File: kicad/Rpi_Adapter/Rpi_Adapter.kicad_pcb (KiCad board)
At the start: 2 copper layers, 65 x 22 mm, 49 parts, among them P1 CONN_02X20, P2 CONN_02X03

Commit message: Created the layout and submitted to OSH Park
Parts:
- removed 1 (x2), 10, 11, 12, 13, 14, 15, 16, 17, 18, 19, 2, 20 (x2), 21 (x2), 22, 23, 24, 25, 26, 27, 28, 29, 3, 30, 31, 32, 33, 34, 35, 36, 37, 38, 39, 4, 40 (x2), 5, 6, 7, 8, 9: Stitch, Rpi_Adapter_Footprints:Stitch
- removed MCU1: RaspberryPi_3b, Rpi_Adapter_Footprints:Pin_Header_Straight_2x20_Pitch2.54mm
- removed MNT** (x2): MountingHole_2.7mm_M2.5, Mounting_Holes:MountingHole_2.7mm_M2.5
- removed P2: CONN_02X03, Pin_Headers:Pin_Header_Straight_2x03_Pitch2.54mm
- added ?: Stitch, Rpi_Adapter_Footprints:Stitch, F.Cu at (169.6, 42.4)
- added ?: Stitch, Rpi_Adapter_Footprints:Stitch, F.Cu at (167.6, 41.5)
- added ?: Stitch, Rpi_Adapter_Footprints:Stitch, F.Cu at (172.2, 37.6)
- added ?: Stitch, Rpi_Adapter_Footprints:Stitch, F.Cu at (169.5, 40.6)
- added ?: Stitch, Rpi_Adapter_Footprints:Stitch, F.Cu at (171.2, 36.6)
- added ?: Stitch, Rpi_Adapter_Footprints:Stitch, F.Cu at (170.6, 39.1)
- added ?: Stitch, Rpi_Adapter_Footprints:Stitch, F.Cu at (169.5, 38.2)
- added ?: Stitch, Rpi_Adapter_Footprints:Stitch, F.Cu at (168.1, 39.8)
- added ?: Stitch, Rpi_Adapter_Footprints:Stitch, F.Cu at (167.7, 43.3)
- added H1: DIGI_XBEE, Rpi_Adapter_Footprints:XBEE_S2C_Short, F.Cu at (176.0, 45.8)
- P1: value CONN_02X20 -> Raspberry PI; footprint Pin_Headers:Pin_Header_Straight_2x20_Pitch2.54mm -> Socket_Strips:Socket_Strip_Straight_2x06_Pitch2.54mm
- moved P1 7.46 mm to (158.8, 47.2)
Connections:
- P1 pad 1: /5V -> /3V3
- P1 pad 10: GND -> /UART0_Rx
- P1 pad 11: /GPIO_18 -> (no net)
- P1 pad 12: /GPIO_17 -> (no net)
- P1 pad 2: /3V3 -> /5V
- P1 pad 3: /5V -> (no net)
- P1 pad 4: /I2C1_SDA -> /5V
- P1 pad 5: GND -> (no net)
- P1 pad 6: /I2C1_SCL -> GND
- P1 pad 7: /UART0_Tx -> (no net)
- P1 pad 8: /GPIO_4 -> /UART0_Tx
- P1 pad 9: /UART0_Rx -> GND
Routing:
- net /I2C1_SCL: track 31.1 -> 0.00 mm
- net /I2C1_SDA: track 31.1 -> 0.00 mm
- net /GPIO_4: track 25.0 -> 0.00 mm
- net /GPIO_5: track 22.6 -> 0.00 mm
- net /GPIO_6: track 22.6 -> 0.00 mm
- net /5V: track 21.1 -> 2.54 mm
- net /3V3: track 40.1 -> 25.4 mm
- net /GPIO_18: track 9.35 -> 0.00 mm
- net /SPI0_SCLK: track 9.30 -> 0.00 mm
- net /SPI0_MISO: track 9.30 -> 0.00 mm
- net /GPIO_27: track 9.30 -> 0.00 mm
- net /GPIO_26: track 9.30 -> 0.00 mm
- net /GPIO_22: track 9.30 -> 0.00 mm
- net /GPIO_19: track 9.30 -> 0.00 mm
- net /SPI0_MOSI: track 9.30 -> 0.00 mm
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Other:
- board size 65 x 22 mm -> 21.5 x 25.5 mm
- board text removed: "GND I2C SCL I2C SDA"
- board text removed: "GPIO6 GPIO5 ~INT"
- board text removed: "Raspberry Pi Expansion and CE Header Adapter"
- board text removed: "Rpi_Adapter 2L_3"

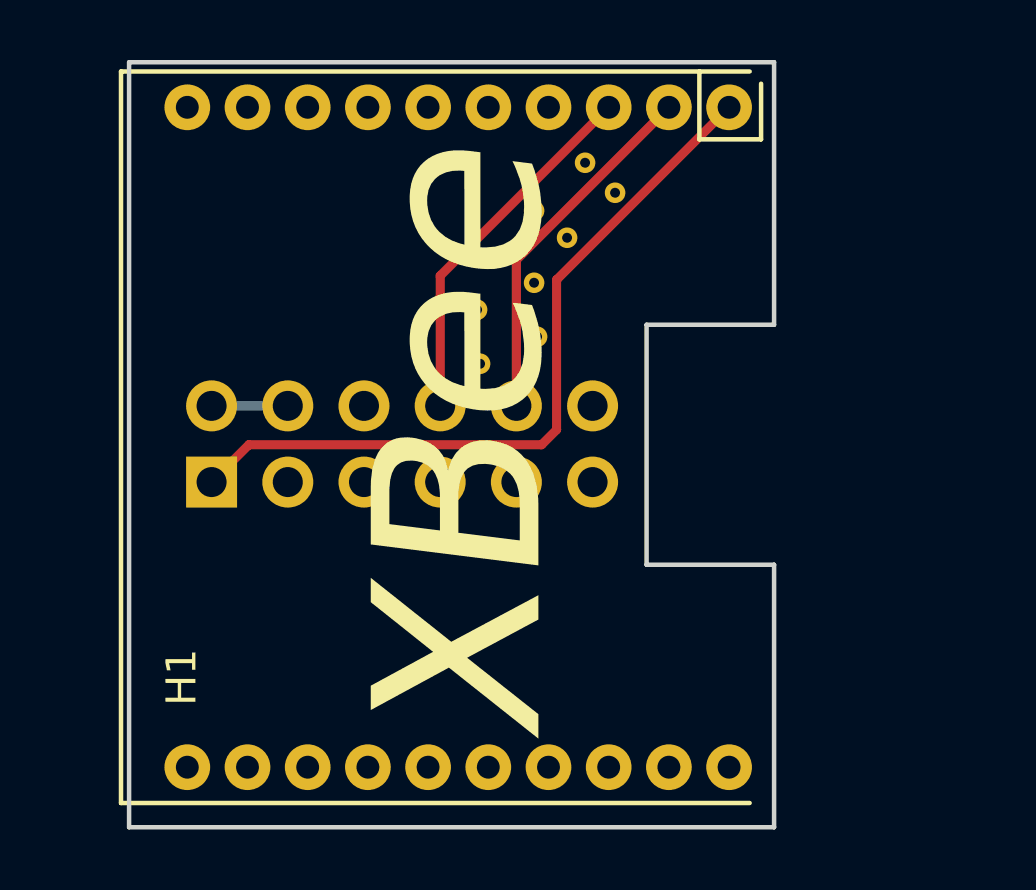
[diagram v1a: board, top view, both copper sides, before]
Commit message: Ads a SGM811 and reference to a shared library
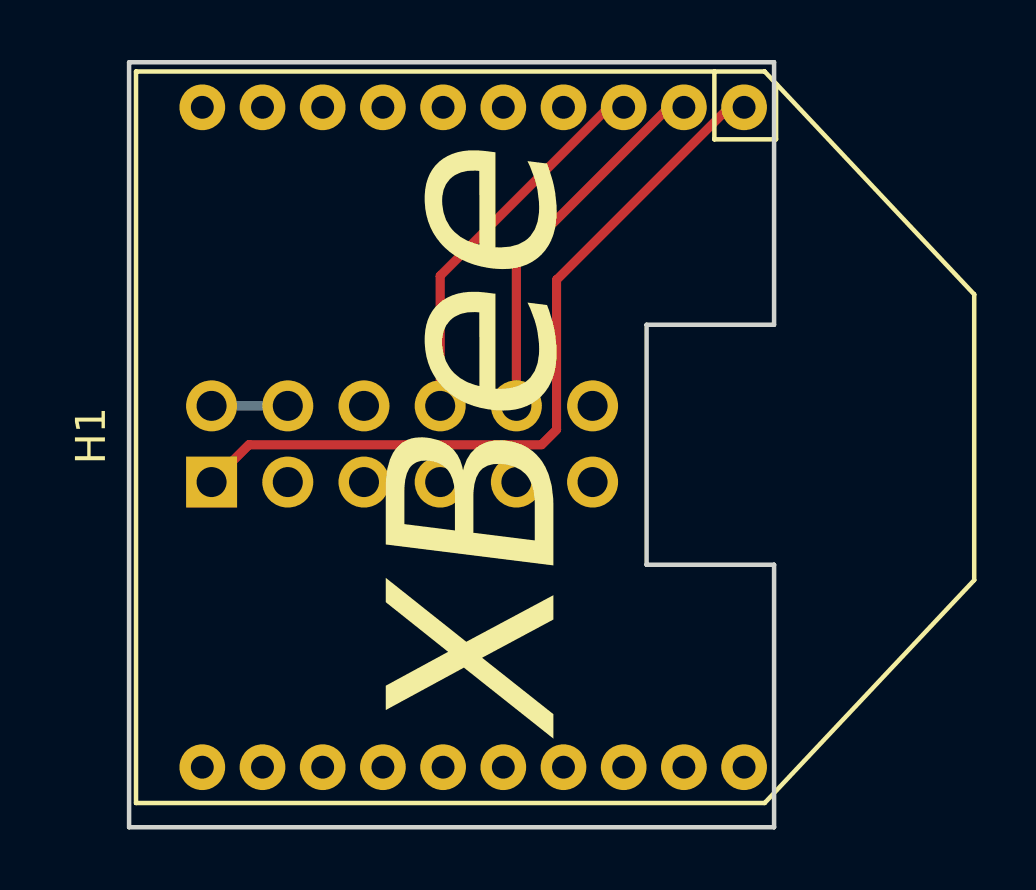
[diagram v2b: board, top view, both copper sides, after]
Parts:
- removed ? (x9): Stitch, Rpi_Adapter_Footprints:Stitch
- H1: footprint Rpi_Adapter_Footprints:XBEE_S2C_Short -> XBee-Adapter:XBEE_S2C
- moved H1 0.50 mm to (176.5, 45.8)

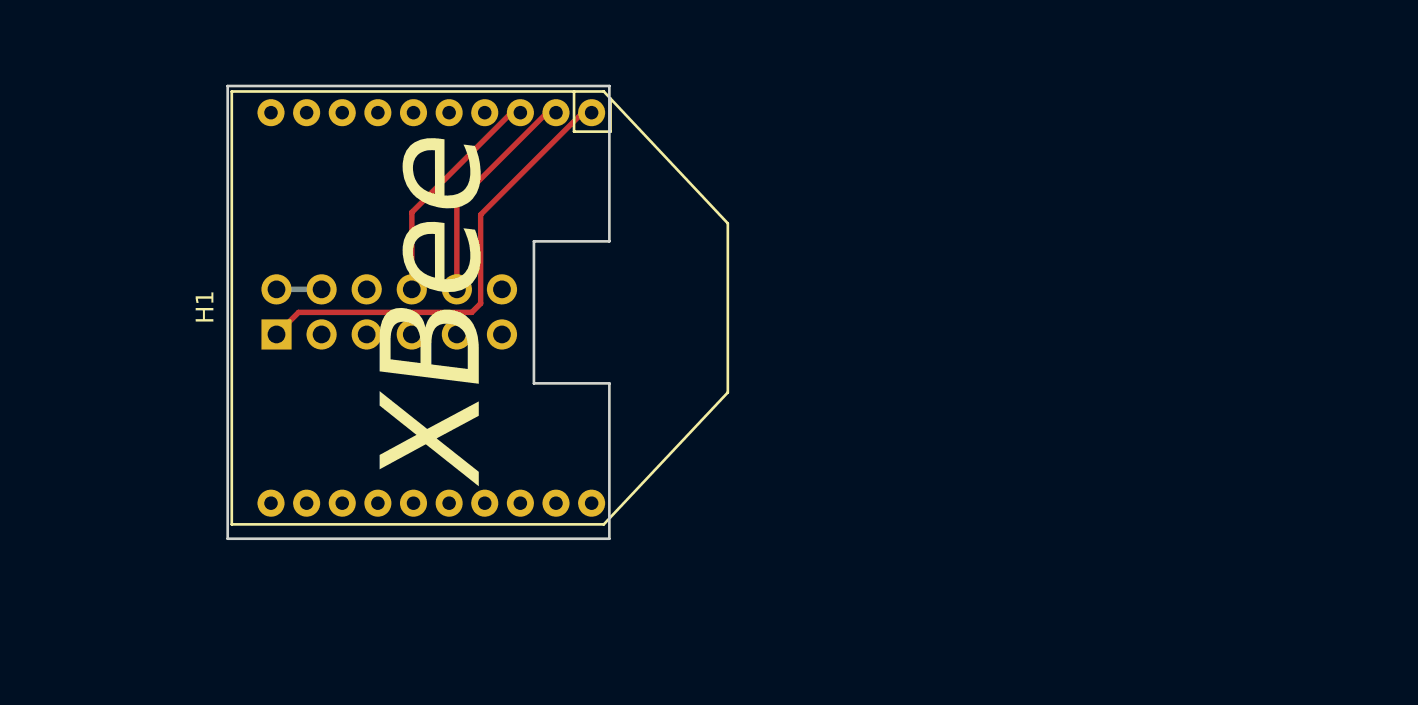
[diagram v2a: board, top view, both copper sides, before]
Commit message: Updated the 3d view and a new layout
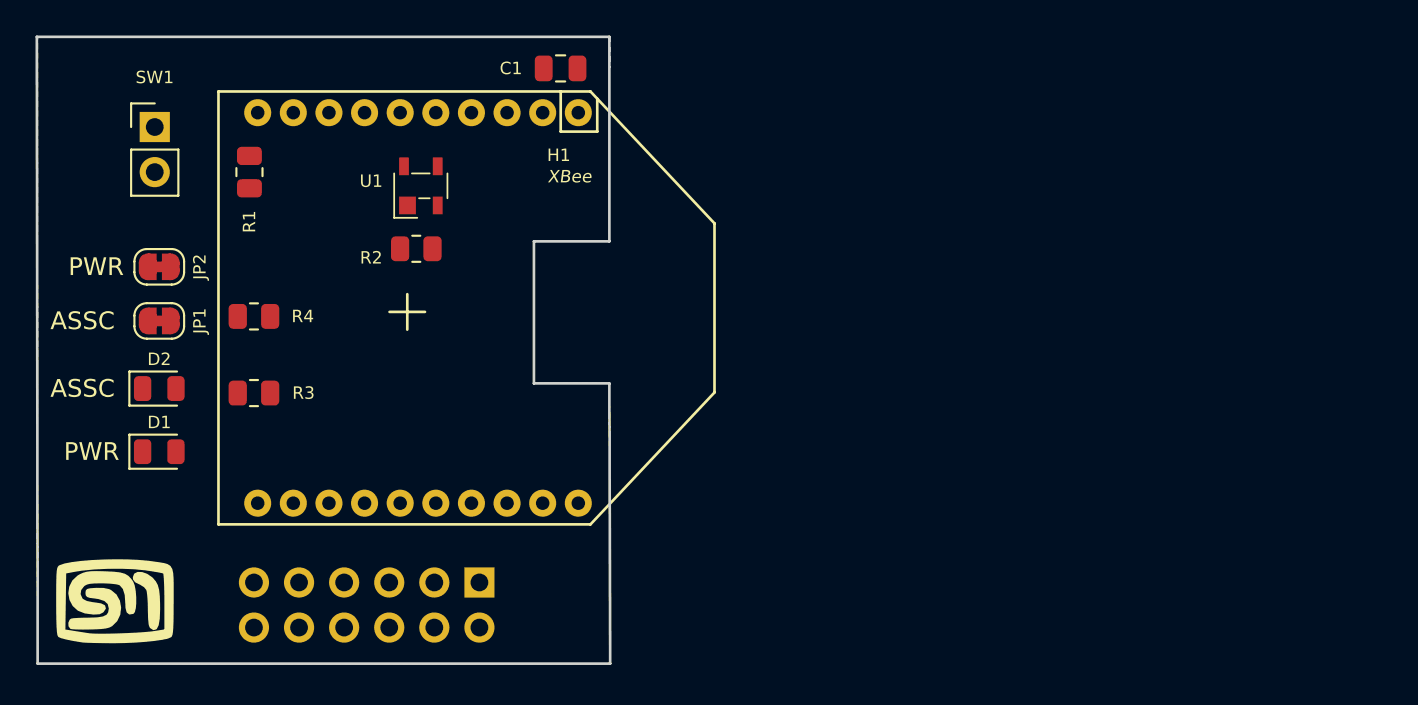
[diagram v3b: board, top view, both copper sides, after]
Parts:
- added B1: XBee Board, mech:Board Ref, F.Cu at (166.1, 46.0)
- added B2: Raspberry Pi Zero, mech:Board Ref, B.Cu at (178.3, 36.1)
- added C1: 100nF, Capacitor_SMD:C_0805_2012Metric, F.Cu at (174.8, 32.3)
- added D1: LED, LED_SMD:LED_0805_2012Metric, F.Cu at (152.1, 53.8)
- added D2: LED, LED_SMD:LED_0805_2012Metric, F.Cu at (152.1, 50.3)
- added JP1: ASSOCIATE, Jumper:SolderJumper-2_P1.3mm_Bridged_RoundedPad1.0x1.5mm, F.Cu at (152.1, 46.5)
- added JP2: ON, Jumper:SolderJumper-2_P1.3mm_Bridged_RoundedPad1.0x1.5mm, F.Cu at (152.1, 43.4)
- added L1: logo, XBee-Adapter:MyBasic_rounded_50_1, F.Cu at (149.6, 62.2)
- added R1: 100kΩ, Resistor_SMD:R_0805_2012Metric, F.Cu at (157.2, 38.1)
- added R2: 100kΩ, Resistor_SMD:R_0805_2012Metric, F.Cu at (166.6, 42.4)
- added R3: 680Ω, Resistor_SMD:R_0805_2012Metric, F.Cu at (157.5, 50.5)
- added R4: 680Ω, Resistor_SMD:R_0805_2012Metric, F.Cu at (157.5, 46.2)
- added SW1: SW_Push, Connector_PinHeader_2.54mm:PinHeader_1x02_P2.54mm_Vertical, F.Cu at (151.9, 35.6)
- added U1: SGM811, GoldCap-Check:SGM811B, F.Cu at (166.9, 38.9)
- moved P1 18.1 mm to (170.2, 61.2), turned to 90 degrees
- moved H1 0.75 mm to (175.8, 45.8)
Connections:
- H1 pad 13: (no net) -> Net-(H1-Pad13)
- H1 pad 15: (no net) -> Net-(H1-Pad15)
- H1 pad 5: (no net) -> /~RESET
- P1 pad 12: (no net) -> /GPIO_18
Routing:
- net /3V3: track 25.4 -> 0.00 mm
- net /UART0_Tx: track 12.3 -> 0.00 mm
- net /UART0_Rx: track 12.1 -> 0.00 mm
- net /5V: track 2.54 -> 0.00 mm
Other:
- board size 21.5 x 25.5 mm -> 32.3 x 35.3 mm
- board text added: "ASSC"
- board text added: "PWR"

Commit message: Initial routing
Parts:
- moved JP1 8.74 mm to (159.3, 41.4)
- moved JP2 8.07 mm to (159.3, 47.2)
- moved L1 6.36 mm to (149.9, 55.9)
- moved D2 5.89 mm to (152.9, 44.5)
- moved D1 3.39 mm to (152.9, 50.5)
- moved R4 2.51 mm to (159.3, 44.5), turned to 180 degrees
- moved R3 1.78 mm to (159.3, 50.5)
- moved R1 1.22 mm to (158.0, 37.1), turned to 0 degrees
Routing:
- net /GPIO_18: track 0.00 -> 46.7 mm
- net /3V3: track 0.00 -> 39.9 mm, vias 0 -> 1
- net /UART0_Rx: track 0.00 -> 39.9 mm
- net /UART0_Tx: track 0.00 -> 33.7 mm
- net Net-(H1-Pad15): track 0.00 -> 17.8 mm
- net Net-(H1-Pad13): track 0.00 -> 10.2 mm
- net /~RESET: track 0.00 -> 8.25 mm
- net Net-(R1-Pad1): track 0.00 -> 5.82 mm
- net Net-(D2-Pad2): track 0.00 -> 4.50 mm
- net Net-(D1-Pad2): track 0.00 -> 4.50 mm
- net Net-(JP2-Pad2): track 0.00 -> 3.95 mm
- net Net-(JP1-Pad2): track 0.00 -> 3.70 mm
- net /5V: track 0.00 -> 2.54 mm
- net GND: vias 0 -> 3
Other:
- outline, holes or cut-outs redrawn
- board text added: "~RESET"

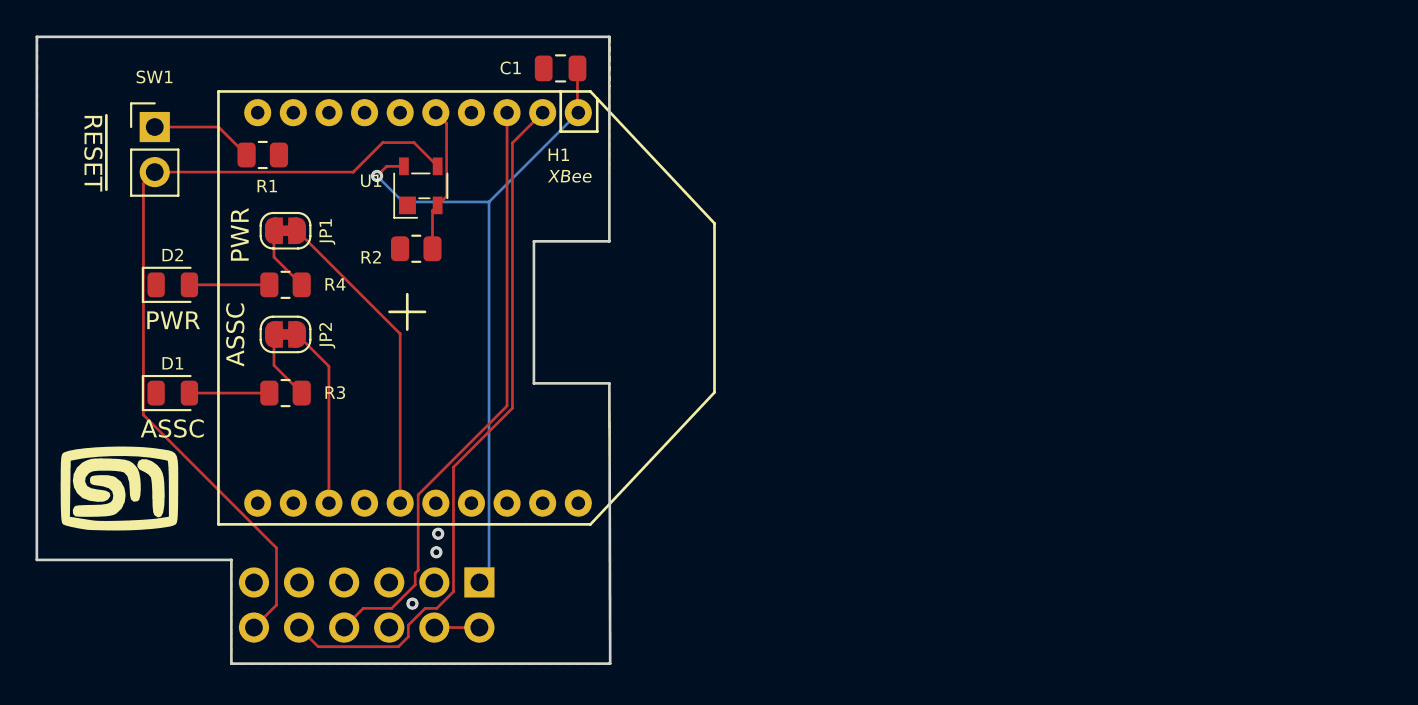
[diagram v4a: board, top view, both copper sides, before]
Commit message: Completed the layout and routing, Sent to OSH Park
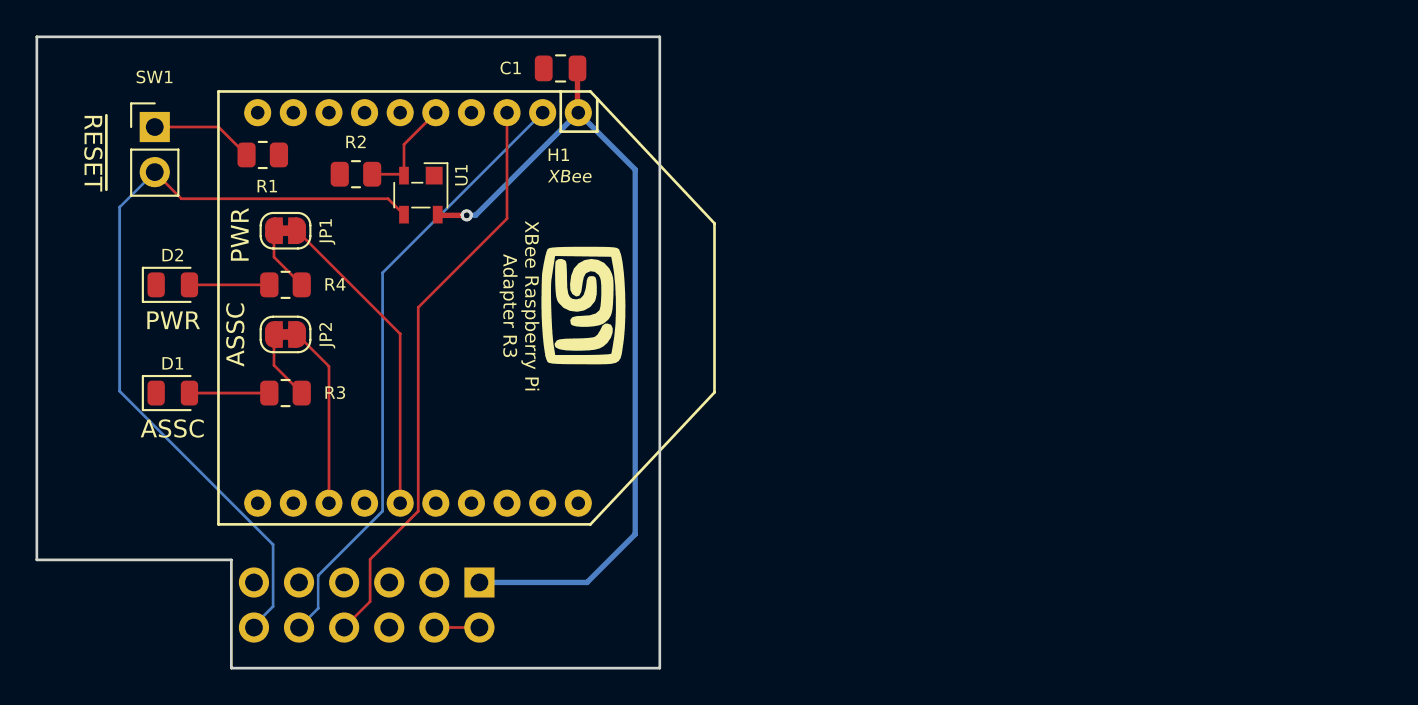
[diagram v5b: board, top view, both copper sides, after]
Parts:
- removed B2: Raspberry Pi Zero, mech:Board Ref
- added Brd2: Raspberry Pi Zero, mech:Board Ref, B.Cu at (178.3, 36.1)
- added Lg2: KiCad, Symbols:KiCad-Logo2_6mm_SilkScreen, B.Cu at (150.0, 45.5)
- added Lg3: logo, XBee-Adapter:MyBasic_rounded_50_1, F.Cu at (176.1, 45.6)
- Lg1: renamed from L1; moved to B.Cu
- moved Lg1 28.1 mm to (176.1, 45.7), turned to 90 degrees
- moved R2 5.40 mm to (163.2, 38.2)
- moved U1 0.52 mm to (166.9, 39.4), turned to 180 degrees
- renumbered B1 to Brd1
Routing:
- net /3V3: track 39.9 -> 47.8 mm
- net /UART0_Rx: track 39.9 -> 34.7 mm
- net /~RESET: track 8.25 -> 6.11 mm
- net /GPIO_18: track 46.7 -> 45.7 mm
- net /UART0_Tx: track 33.7 -> 32.8 mm
- net GND: vias 3 -> 0
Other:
- board size 32.3 x 35.3 mm -> 35.1 x 35.6 mm
- board text added: "XBee Raspberry Pi Adapter R3"
